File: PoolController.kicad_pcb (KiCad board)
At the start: 2 copper layers, 80 x 75 mm, 23 parts, among them J1 RJ12, J2 RJ12, J3 Header, J4 Conn_02x12_Counter_Clockwise, Q1 MMBT3904, U1 LM2678S-5.0/NOPB

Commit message: ### Changed - Rev 11 - changed RJ12 connectors to 5324 6P6C pieces and updated pcb - Rev 11 - additional gnd connecting vias under buck (U1)
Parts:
- J1, J2: footprint Connector_RJ:RJ25_Wayconn_MJEA-660X1_Horizontal -> Connector_RJ:RJ25_RJ12_5324_mini
- moved J1 1.55 mm to (77.3, 80.0)
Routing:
- net GND (from connector): track 206.5 -> 172.6 mm, vias 3 -> 7
- net Net-(J3-Pin_3): track 81.9 -> 69.2 mm
- net +24V (from connector): track 54.6 -> 49.9 mm

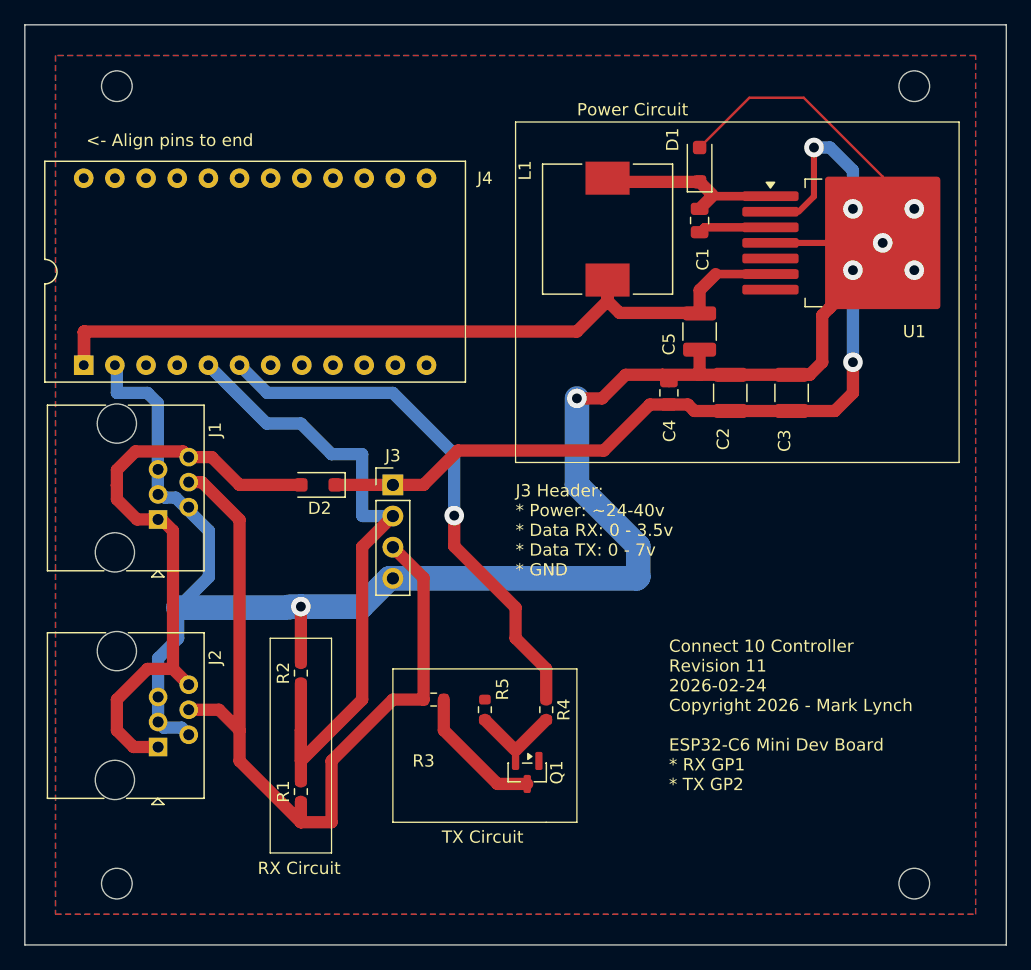
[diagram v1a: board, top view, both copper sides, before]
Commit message: ## [0.10.2] - 2026-03-15 ### Changed - Rev 12 - fixed error in connecting vias shorting gnd to Net D2-K - Rev 12 - tidy up routing of D2
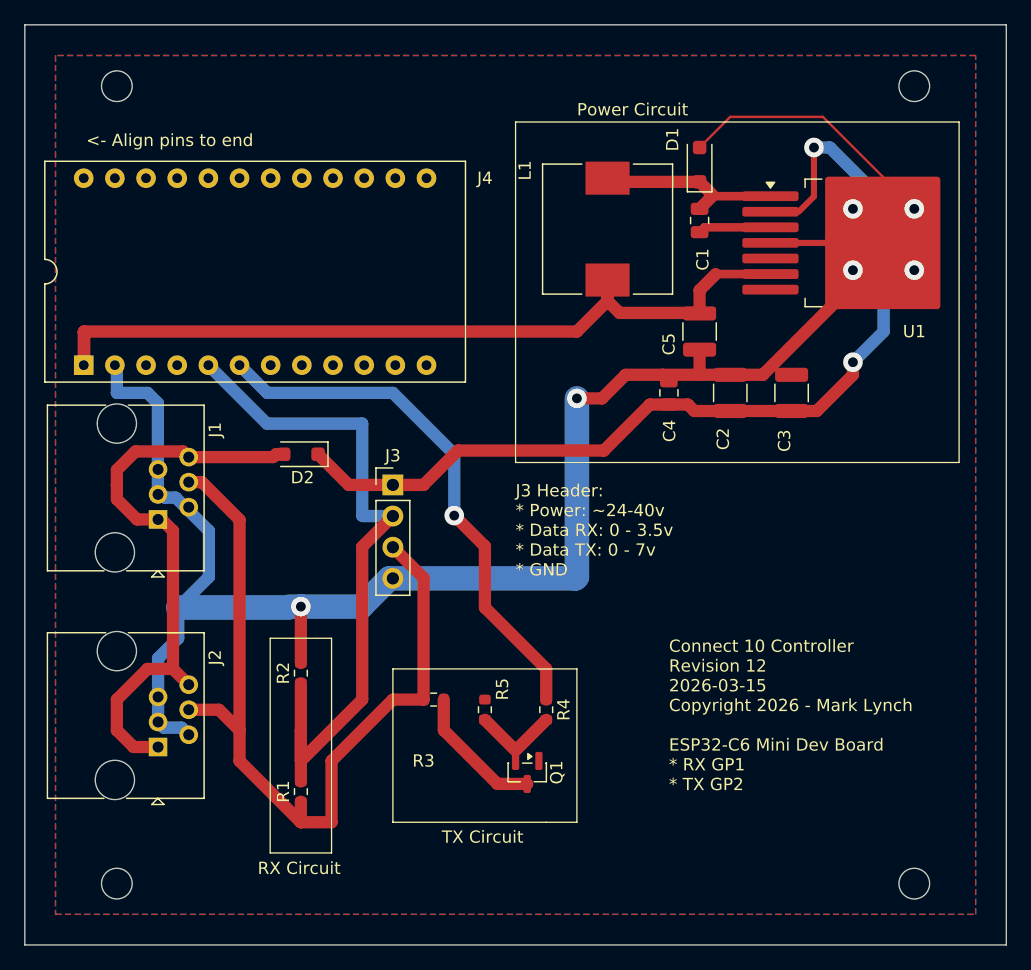
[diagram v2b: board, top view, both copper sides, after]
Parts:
- moved D2 2.87 mm to (87.5, 75.0)
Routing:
- net GND (from connector): track 172.6 -> 156.4 mm, vias 7 -> 6
- net Net-(D2-K): track 75.9 -> 79.5 mm
- net +24V (from connector): track 49.9 -> 47.7 mm
- net Net-(J3-Pin_2): track 56.6 -> 58.1 mm

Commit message: Version 1.0.0 - Rev 13 of board.
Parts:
- Q1: footprint Package_TO_SOT_SMD:SOT-23 -> MMBT3904:SOT-23_MCC
- moved R5 7.70 mm to (107.5, 101.7), turned to 90 degrees
- moved Q1 4.37 mm to (101.6, 101.5), turned to 90 degrees
- moved R3 2.63 mm to (97.5, 97.5), turned to -90 degrees
- moved R2 2.16 mm to (87.5, 95.0)
- moved R1 1.67 mm to (87.5, 100.8)
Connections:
- Q1 pad 1: GND (from connector) -> Net-(Q1-B)
- Q1 pad 2: Net-(Q1-B) -> GND (from connector)
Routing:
- net GND (from connector): track 156.4 -> 164.2 mm, vias 6 -> 7
- net Net-(J3-Pin_2): track 58.1 -> 50.7 mm
- net Net-(Q1-C): track 11.1 -> 5.94 mm
- net Net-(Q1-B): track 6.94 -> 9.88 mm
- net Net-(J3-Pin_3): track 69.2 -> 66.7 mm
